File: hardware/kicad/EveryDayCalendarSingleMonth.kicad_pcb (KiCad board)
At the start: 2 copper layers, 100 x 100 mm, 143 parts, among them J2_POWER_IN1 Conn_01x02, J3_PROGRAMING_PIN1 Conn_01x06, Q1 PN2222A, Q2 PN2222A, U1 74AHC1G125

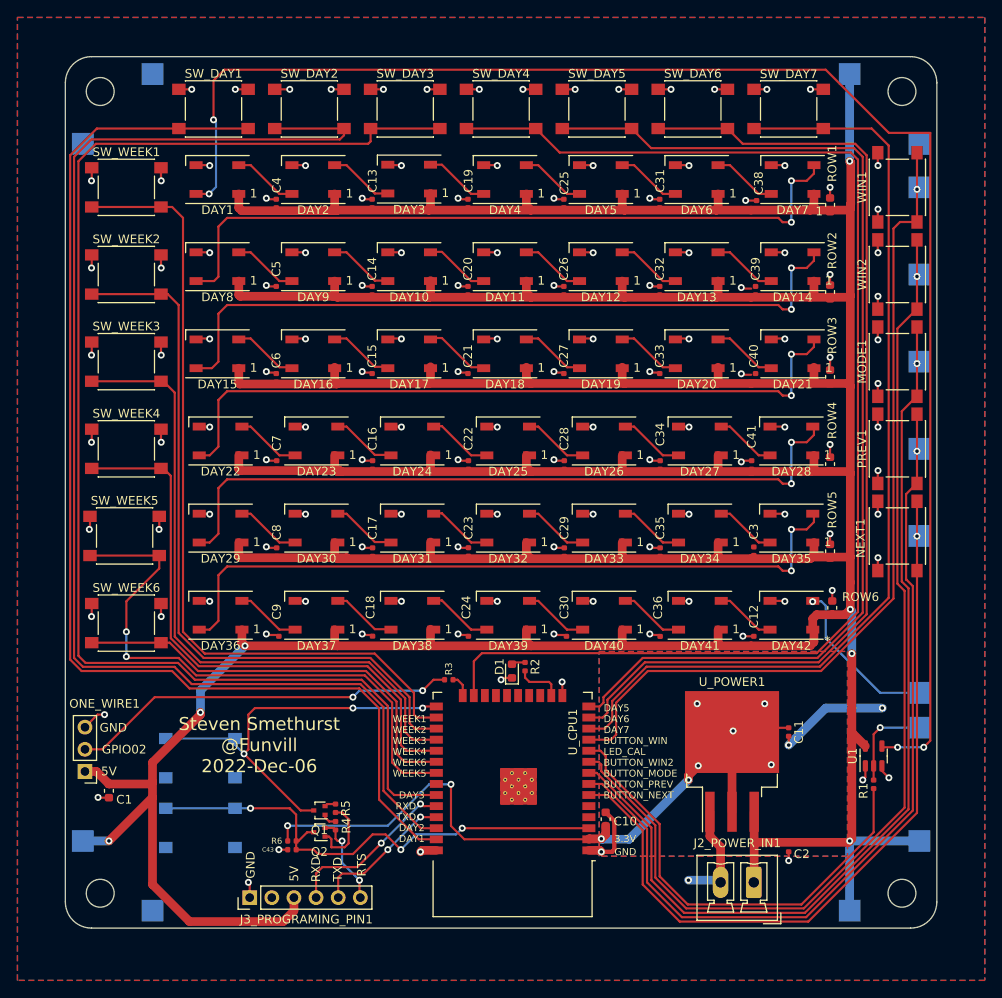
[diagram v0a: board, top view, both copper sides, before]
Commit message: Moved the LEDs slightly and resubmitted to JLPCB
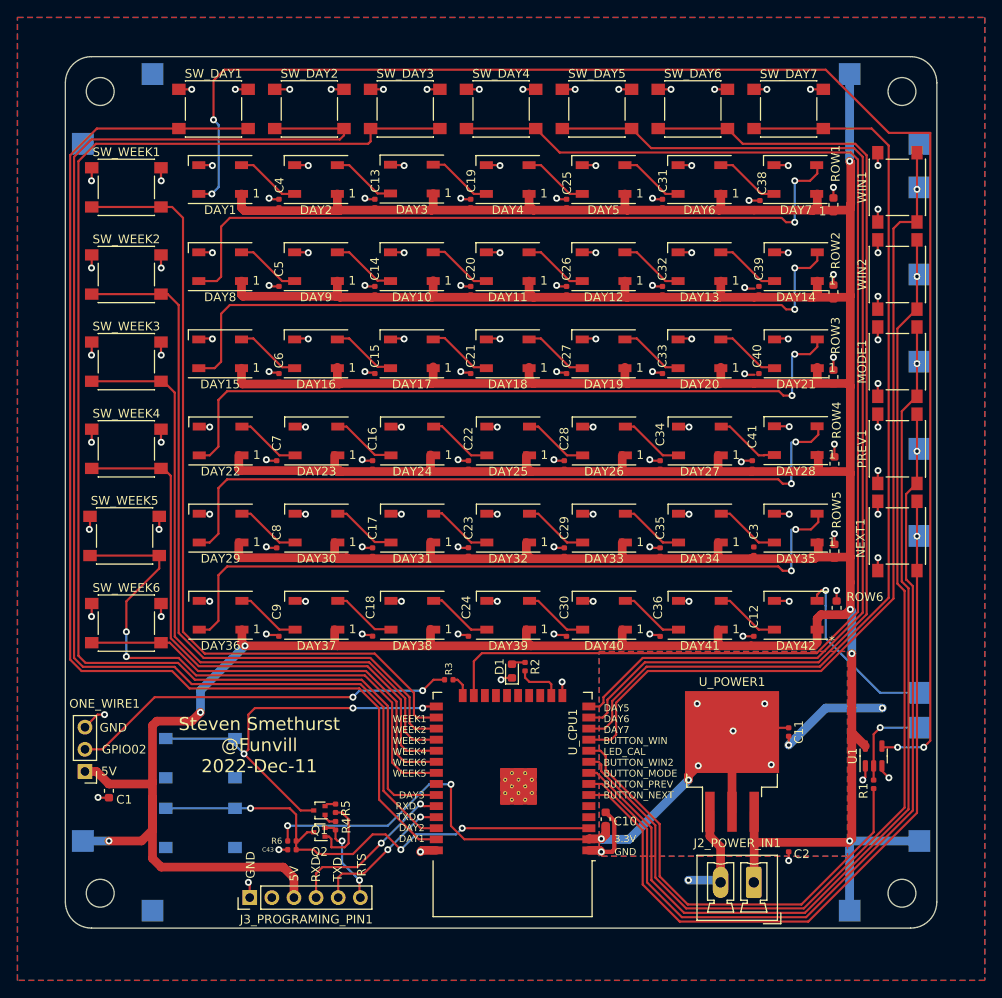
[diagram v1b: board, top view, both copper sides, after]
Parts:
- moved DAY28 0.50 mm to (133.8, 84.1)
- moved ROW4 0.50 mm to (138.2, 86.7)
- moved DAY35 0.50 mm to (133.8, 94.1)
- moved DAY42 0.50 mm to (133.8, 104.1)
- moved ROW5 0.50 mm to (138.2, 96.8)
- moved ROW6 0.50 mm to (138.5, 103.2)
- moved C39 0.39 mm to (129.6, 66.8)
- moved C40 0.39 mm to (129.6, 76.8)
- moved DAY14 0.39 mm to (133.8, 64.1)
- moved DAY21 0.39 mm to (133.8, 74.1)
- moved C38 0.38 mm to (129.7, 57.0)
- moved ROW1 0.38 mm to (138.1, 57.0)
- moved ROW2 0.38 mm to (138.1, 67.0)
- moved ROW3 0.38 mm to (138.1, 76.8)
- moved C13 0.31 mm to (85.5, 56.9)
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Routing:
- net Net-(DAY42-Pad2): track 18.8 -> 20.7 mm
- net +5V: track 702.6 -> 703.5 mm
- net Net-(DAY27-Pad2): track 7.47 -> 7.98 mm
- net Net-(DAY34-Pad2): track 7.47 -> 7.97 mm
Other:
- board text added: "Steven Smethurst @Funvill 2022-Dec-11"
- board text removed: "Steven Smethurst @Funvill 2022-Dec-06"
